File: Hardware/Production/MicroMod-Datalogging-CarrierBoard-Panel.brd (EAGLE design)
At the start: 150.1 x 177.8 mm, 1190 parts, among them J100 QWIIC_RIGHT_ANGLE, J101 JTAG, J102 Dedicated, J104 microSD, J105 I2C, J108 SPI, J109 UART, J11 microSD, J110 MICROMOD-2222-C, J12 SPI, J14 I2C, J16 QWIIC_RIGHT_ANGLE, J17 JTAG, J18 Dedicated, J2 JTAG, J20 microSD, J21 I2C, J24 SPI, J25 UART, J26 MICROMOD-2222-C, J3 QWIIC_RIGHT_ANGLE, J30 QWIIC_RIGHT_ANGLE, J31 JTAG, J32 Dedicated, J34 microSD, J35 I2C, J38 SPI, J39 UART, J40 MICROMOD-2222-C, J44 QWIIC_RIGHT_ANGLE, J45 JTAG, J46 Dedicated, J48 microSD, J49 I2C, J5 UART, J52 SPI, J53 UART, J54 MICROMOD-2222-C, J58 QWIIC_RIGHT_ANGLE, J59 JTAG, J6 MICROMOD-2222-C, J60 Dedicated, J62 microSD, J63 I2C, J66 SPI, J67 UART, J68 MICROMOD-2222-C, J72 QWIIC_RIGHT_ANGLE, J73 JTAG, J74 Dedicated, J76 microSD, J77 I2C, J8 Dedicated, J80 SPI, J81 UART, J82 MICROMOD-2222-C, J86 QWIIC_RIGHT_ANGLE, J87 JTAG, J88 Dedicated, J90 microSD, J91 I2C, J94 SPI, J95 UART, J96 MICROMOD-2222-C, U1 3.3V, U10 MCP73831, U11 3.3V, U12 3.3V, U13 AP7361C-33, U14 MCP73831, U15 3.3V, U16 3.3V, U17 AP7361C-33, U18 MCP73831, U19 3.3V, U2 MCP73831, U20 3.3V, U21 AP7361C-33, U22 MCP73831, U23 3.3V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

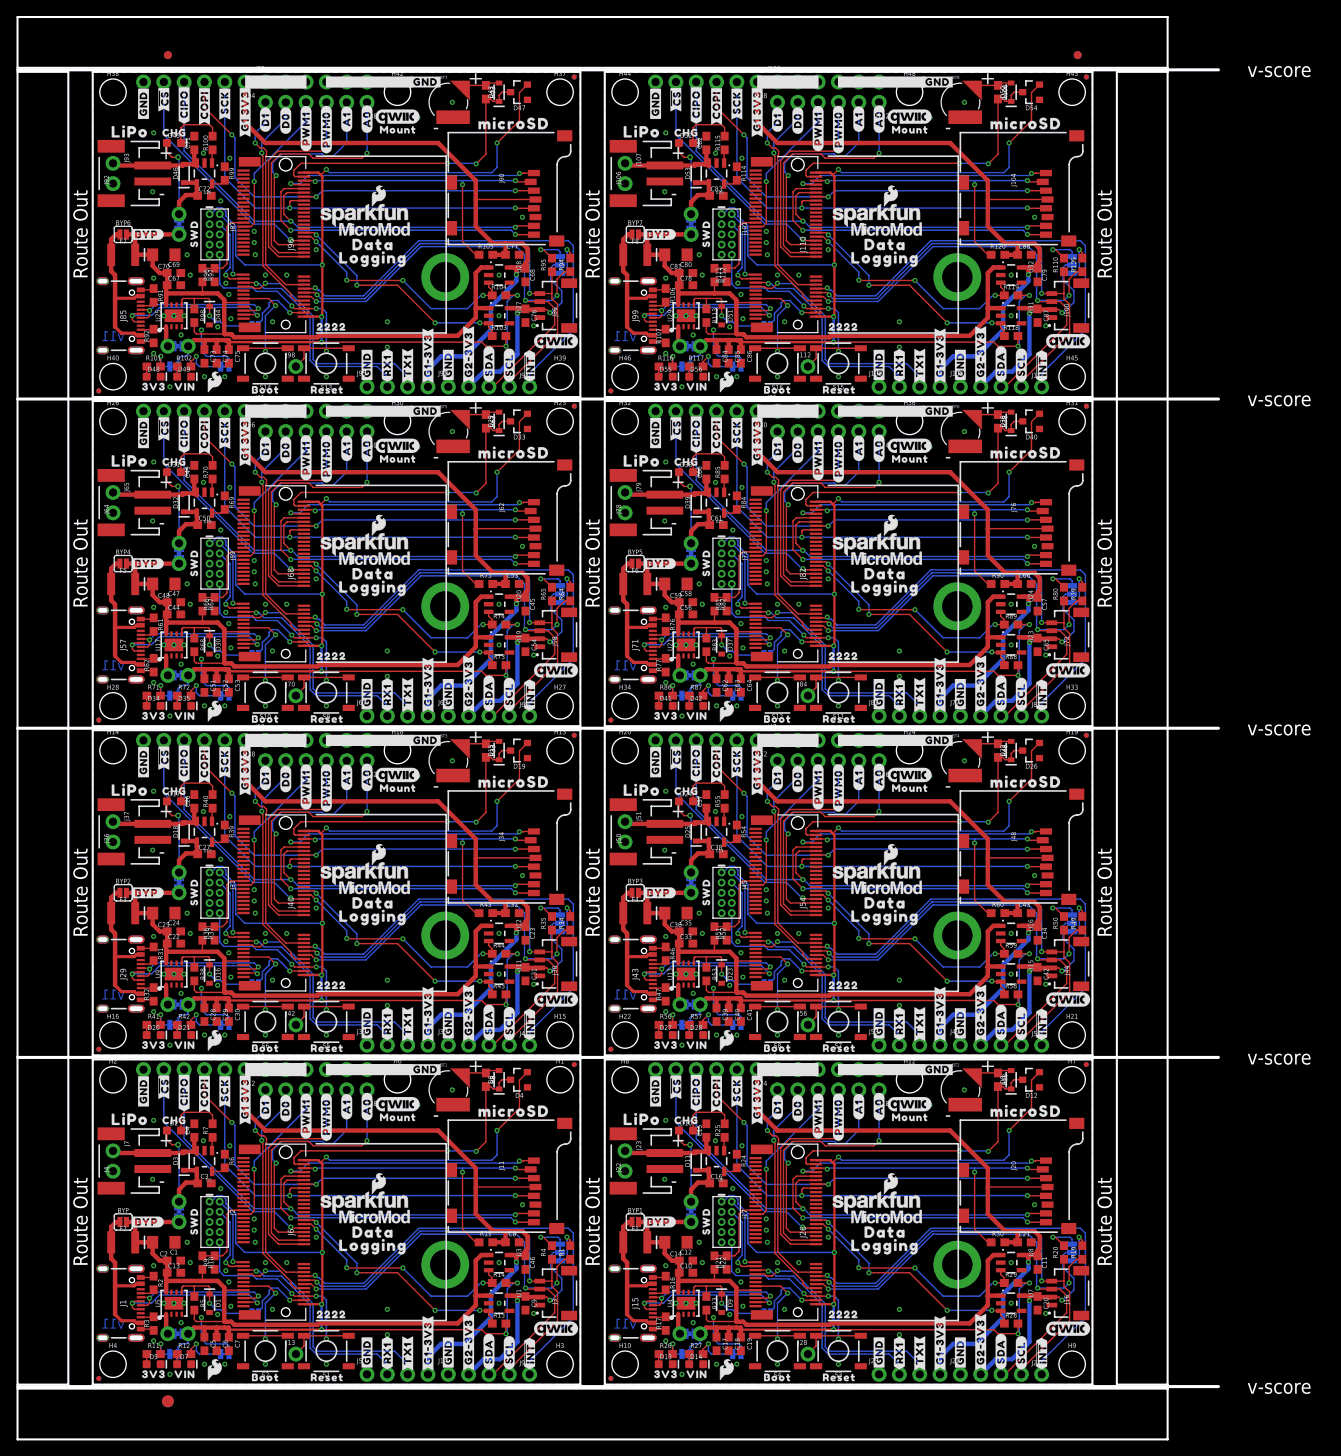
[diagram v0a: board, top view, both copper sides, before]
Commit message: Change SD to pure SPI connection.
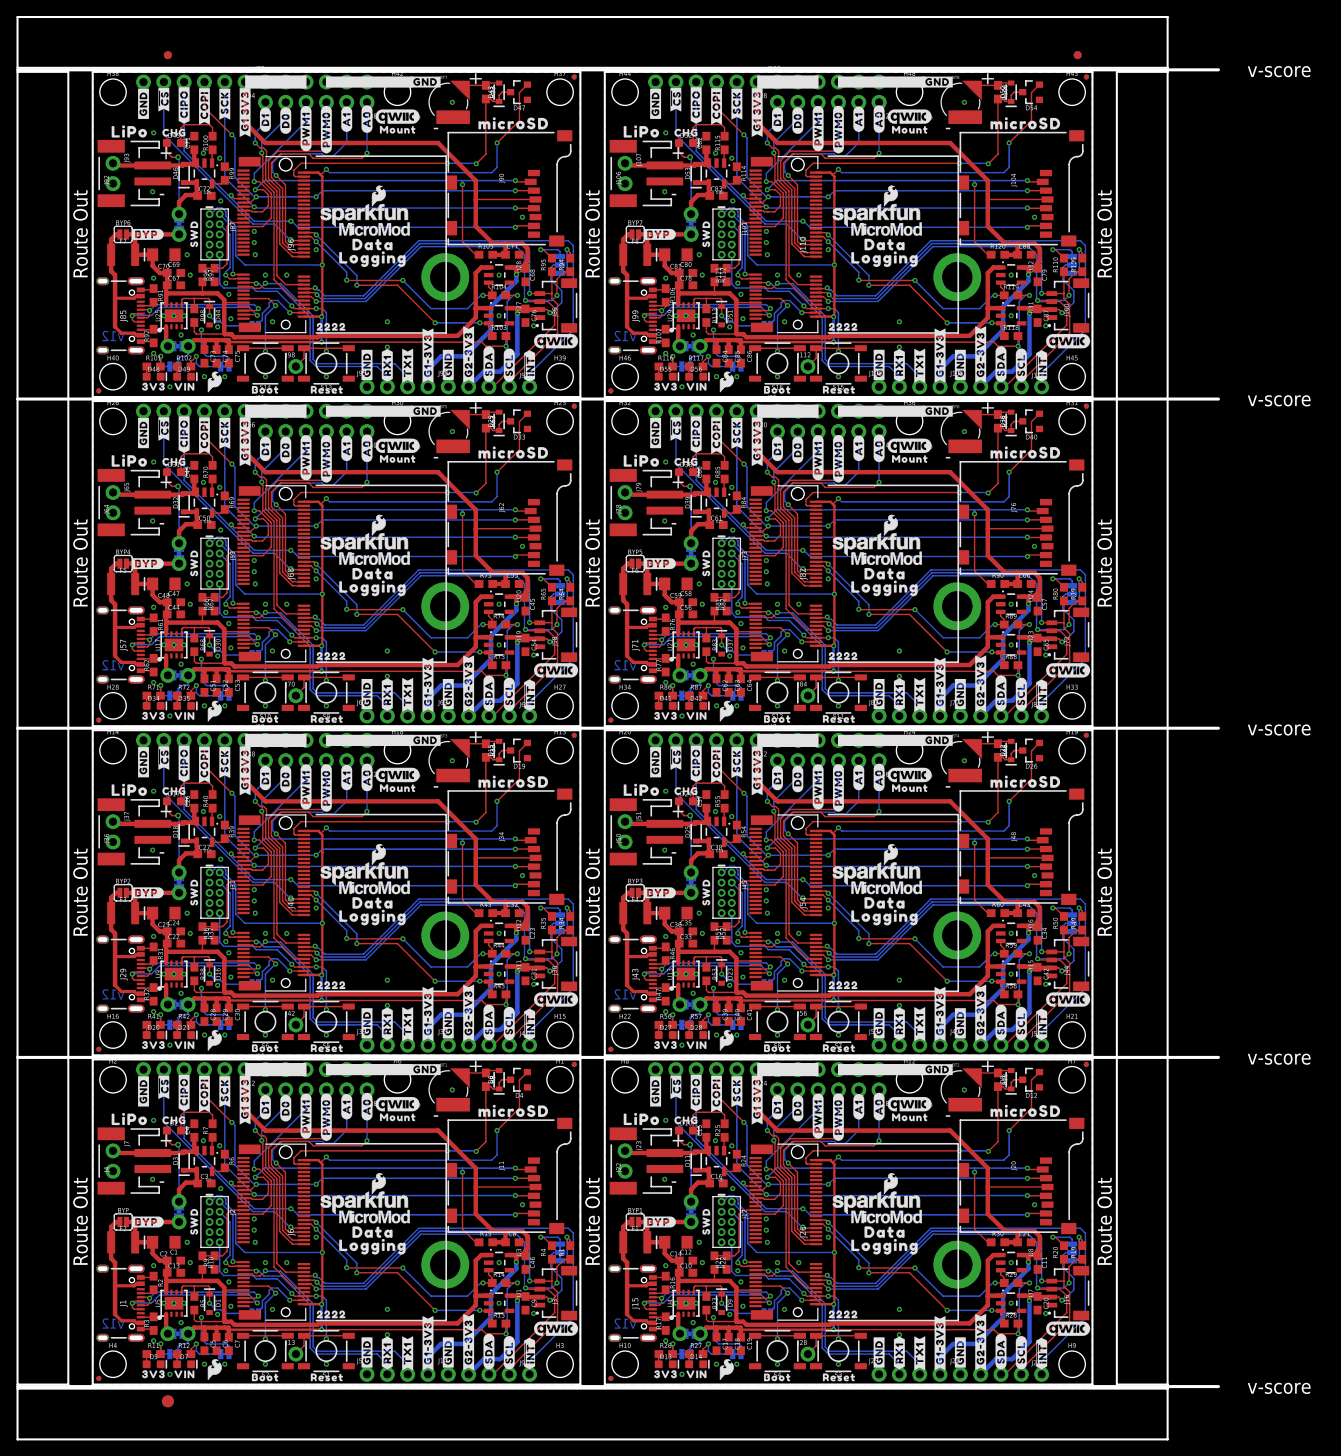
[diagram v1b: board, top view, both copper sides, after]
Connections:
- removed net SD_DAT1: J11.DAT1, J6.66
- removed net SD_DAT10: J62.DAT2, J68.68
- removed net SD_DAT11: J76.DAT1, J82.66
- removed net SD_DAT12: J76.DAT2, J82.68
- removed net SD_DAT13: J90.DAT1, J96.66
- removed net SD_DAT14: J90.DAT2, J96.68
- removed net SD_DAT15: J104.DAT1, J110.66
- removed net SD_DAT16: J104.DAT2, J110.68
- removed net SD_DAT2: J11.DAT2, J6.68
- removed net SD_DAT3: J20.DAT1, J26.66
- removed net SD_DAT4: J20.DAT2, J26.68
- removed net SD_DAT5: J34.DAT1, J40.66
- removed net SD_DAT6: J34.DAT2, J40.68
- removed net SD_DAT7: J48.DAT1, J54.66
- removed net SD_DAT8: J48.DAT2, J54.68
- removed net SD_DAT9: J62.DAT1, J68.66
- net SD_!CS!: now also J6.55; no longer J6.70
- net SD_!CS!1: now also J26.55; no longer J26.70
- net SD_!CS!2: now also J40.55; no longer J40.70
- net SD_!CS!3: now also J54.55; no longer J54.70
- net SD_!CS!4: now also J68.55; no longer J68.70
- net SD_!CS!5: now also J82.55; no longer J82.70
- net SD_!CS!6: now also J96.55; no longer J96.70
- net SD_!CS!7: now also J110.55; no longer J110.70
- net SPI_CIPO: now also J6.61; no longer J6.64
- net SPI_CIPO1: now also J26.61; no longer J26.64
- net SPI_CIPO2: now also J40.61; no longer J40.64
- net SPI_CIPO3: now also J54.61; no longer J54.64
- net SPI_CIPO4: now also J68.61; no longer J68.64
- net SPI_CIPO5: now also J82.61; no longer J82.64
- net SPI_CIPO6: now also J96.61; no longer J96.64
- net SPI_CIPO7: now also J110.61; no longer J110.64
- net SPI_COPI: now also J6.59; no longer J6.62
- net SPI_COPI1: now also J26.59; no longer J26.62
- net SPI_COPI2: now also J40.59; no longer J40.62
- net SPI_COPI3: now also J54.59; no longer J54.62
- net SPI_COPI4: now also J68.59; no longer J68.62
- net SPI_COPI5: now also J82.59; no longer J82.62
- net SPI_COPI6: now also J96.59; no longer J96.62
- net SPI_COPI7: now also J110.59; no longer J110.62
- net SPI_SCK: now also J6.57; no longer J6.60
- net SPI_SCK1: now also J26.57; no longer J26.60
- net SPI_SCK2: now also J40.57; no longer J40.60
- net SPI_SCK3: now also J54.57; no longer J54.60
- net SPI_SCK4: now also J68.57; no longer J68.60
- net SPI_SCK5: now also J82.57; no longer J82.60
- net SPI_SCK6: now also J96.57; no longer J96.60
- net SPI_SCK7: now also J110.57; no longer J110.60
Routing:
- net SD_DAT15: track 39.0 -> 0.00 mm, vias 2 -> 0
- net SD_DAT13: track 39.0 -> 0.00 mm, vias 2 -> 0
- net SD_DAT9: track 39.0 -> 0.00 mm, vias 2 -> 0
- net SD_DAT11: track 39.0 -> 0.00 mm, vias 2 -> 0
- net SD_DAT3: track 39.0 -> 0.00 mm, vias 2 -> 0
- net SD_DAT1: track 39.0 -> 0.00 mm, vias 2 -> 0
- net SD_DAT5: track 39.0 -> 0.00 mm, vias 2 -> 0
- net SD_DAT7: track 39.0 -> 0.00 mm, vias 2 -> 0
- net SD_DAT8: track 32.7 -> 0.00 mm, vias 2 -> 0
- net SD_DAT6: track 32.7 -> 0.00 mm, vias 2 -> 0
- net SD_DAT4: track 32.7 -> 0.00 mm, vias 2 -> 0
- net SD_DAT16: track 32.7 -> 0.00 mm, vias 2 -> 0
- net SD_DAT2: track 32.7 -> 0.00 mm, vias 2 -> 0
- net SD_DAT14: track 32.7 -> 0.00 mm, vias 2 -> 0
- net SD_DAT12: track 32.7 -> 0.00 mm, vias 2 -> 0
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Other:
- board text added: "v12"
- board text removed: "v11"
